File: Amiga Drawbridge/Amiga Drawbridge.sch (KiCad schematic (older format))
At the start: 13 parts, among them J1 FDC, J2 PWR_EXT, J3 PWR_DRV, J4 12v, M1 Mounting, M2 Mounting, M3 Mounting, M4 Mounting

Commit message: Added metal details
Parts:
- J1: footprint (none) -> Connector_IDC:IDC-Header_2x17_P2.54mm_Vertical
- J2: footprint (none) -> Connector_BarrelJack:BarrelJack_Horizontal
- J3: footprint (none) -> TerminalBlock:TerminalBlock_bornier-4_P5.08mm
- J4: footprint (none) -> Connector_PinSocket_2.54mm:PinSocket_1x01_P2.54mm_Vertical
- JP1, JP2: footprint (none) -> solder_bridge:select
- M1, M2, M3, M4: footprint (none) -> mounting:M3
- R1: footprint (none) -> Resistor_THT:R_Axial_DIN0207_L6.3mm_D2.5mm_P10.16mm_Horizontal
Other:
- note added: "Arduino pin order (A or B):\n1-2 DTR TXO RXI VCC GND GND\n2-3 GND GND VCC RXI TXO DTR"
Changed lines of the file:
@@
 F 0 "J1" H 10050 4865 50  0000 C CNN
 F 1 "FDC" H 10050 4774 50  0000 C CNN
-F 2 "" H 10150 3825 50  0001 C CNN
+F 2 "Connector_IDC:IDC-Header_2x17_P2.54mm_Vertical" H 10150 3825 50  0001 C CNN
 F 3 "~" H 10150 3825 50  0001 C CNN
 	1    10050 3825
@@
 F 0 "R1" H 9234 2896 50  0000 L CNN
 F 1 "1k" H 9234 2805 50  0000 L CNN
-F 2 "" H 9175 2850 50  0001 C CNN
+F 2 "Resistor_THT:R_Axial_DIN0207_L6.3mm_D2.5mm_P10.16mm_Horizontal" H 9175 2850 50  0001 C CNN
 F 3 "~" H 9175 2850 50  0001 C CNN
 	1    9175 2850
@@
 F 0 "JP1" H 6625 3011 50  0000 C CNN
 F 1 "ARD_TYPE" H 6625 3102 50  0000 C CNN
-F 2 "" H 6625 2900 50  0001 C CNN
+F 2 "solder_bridge:select" H 6625 2900 50  0001 C CNN
 F 3 "~" H 6625 2900 50  0001 C CNN
 	1    6625 2900
@@
 F 0 "M1" H 10750 675 50  0001 C CNN
 F 1 "Mounting" H 10750 500 50  0001 C CNN
-F 2 "" H 10750 575 50  0001 C CNN
+F 2 "mounting:M3" H 10750 575 50  0001 C CNN
 F 3 "~" H 10750 575 50  0001 C CNN
 	1    10750 575
@@
 F 0 "M2" H 10875 675 50  0001 C CNN
 F 1 "Mounting" H 10875 500 50  0001 C CNN
-F 2 "" H 10875 575 50  0001 C CNN
+F 2 "mounting:M3" H 10875 575 50  0001 C CNN
 F 3 "~" H 10875 575 50  0001 C CNN
 	1    10875 575
@@
 F 0 "M3" H 11000 675 50  0001 C CNN
 F 1 "Mounting" H 11000 500 50  0001 C CNN
-F 2 "" H 11000 575 50  0001 C CNN
+F 2 "mounting:M3" H 11000 575 50  0001 C CNN
 F 3 "~" H 11000 575 50  0001 C CNN
 	1    11000 575
@@
 F 0 "M4" H 11125 675 50  0001 C CNN
 F 1 "Mounting" H 11125 500 50  0001 C CNN
-F 2 "" H 11125 575 50  0001 C CNN
+F 2 "mounting:M3" H 11125 575 50  0001 C CNN
 F 3 "~" H 11125 575 50  0001 C CNN
 	1    11125 575
@@
 F 0 "J3" H 3398 6666 50  0000 L CNN
 F 1 "PWR_DRV" H 3398 6575 50  0000 L CNN
-F 2 "" H 3050 6675 50  0001 C CNN
+F 2 "TerminalBlock:TerminalBlock_bornier-4_P5.08mm" H 3050 6675 50  0001 C CNN
 F 3 "~" H 3050 6675 50  0001 C CNN
 	1    3050 6675
@@
 F 0 "J2" H 1882 6392 50  0000 C CNN
 F 1 "PWR_EXT" H 1882 6301 50  0000 C CNN
-F 2 "" H 1875 6035 50  0001 C CNN
+F 2 "Connector_BarrelJack:BarrelJack_Horizontal" H 1875 6035 50  0001 C CNN
 F 3 "~" H 1875 6035 50  0001 C CNN
 	1    1825 6075
@@
 F 0 "JP2" H 2525 6179 50  0000 C CNN
 F 1 "PWR_SEL" H 2525 6088 50  0000 C CNN
-F 2 "" H 2525 5975 50  0001 C CNN
+F 2 "solder_bridge:select" H 2525 5975 50  0001 C CNN
 F 3 "~" H 2525 5975 50  0001 C CNN
 	1    2525 5975
@@
 Wire Wire Line
 	2200 6775 2200 7000
-Wire Bus Line
-	4050 2100 4050 3825
-Wire Bus Line
-	8150 2100 8150 4525
-Wire Bus Line
-	4800 2100 4800 4525
-Wire Bus Line
-	8925 2100 8925 4525
 $Comp
 L Connector_Generic:Conn_01x01 J4
@@
 F 0 "J4" H 2730 6917 50  0000 L CNN
 F 1 "12v" H 2730 6826 50  0000 L CNN
-F 2 "" H 2650 6875 50  0001 C CNN
+F 2 "Connector_PinSocket_2.54mm:PinSocket_1x01_P2.54mm_Vertical" H 2650 6875 50  0001 C CNN
 F 3 "~" H 2650 6875 50  0001 C CNN
 	1    2650 6875
 	-1   0    0    1
 $EndComp
+Text Notes 6900 3175 0    50   ~ 0
+Arduino pin order (A or B):\n1-2 DTR TXO RXI VCC GND GND\n2-3 GND GND VCC RXI TXO DTR
+Wire Bus Line
+	4050 2100 4050 3825
+Wire Bus Line
+	8150 2100 8150 4525
+Wire Bus Line
+	4800 2100 4800 4525
+Wire Bus Line
+	8925 2100 8925 4525
 $EndSCHEMATC

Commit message: Arduino Pro Mini footprint
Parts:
- A1: footprint (none) -> arduino:Arduino_Pro_Mini
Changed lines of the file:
@@
 F 0 "A1" H 6525 4025 50  0000 C CNN
 F 1 "Arduino_Pro_Mini" H 6525 3925 50  0000 C CNN
-F 2 "" H 6475 4025 50  0001 C CNN
+F 2 "arduino:Arduino_Pro_Mini" H 6475 4025 50  0001 C CNN
 F 3 "~" H 6475 4025 50  0001 C CNN
 	1    6525 4025

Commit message: Routed tracks
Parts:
- A2: footprint (none) -> ft232rl:FT232RL
- J3: footprint TerminalBlock:TerminalBlock_bornier-4_P5.08mm -> pwr_drv:PWR_DRV
- J4: footprint Connector_PinSocket_2.54mm:PinSocket_1x01_P2.54mm_Vertical -> Connector_PinHeader_2.54mm:PinHeader_1x01_P2.54mm_Vertical
- M1, M2, M3, M4: footprint mounting:M3 -> mounting:M3_pin
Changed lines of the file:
@@
 F 0 "A2" H 2400 4415 50  0000 C CNN
 F 1 "FT232RL" H 2400 4324 50  0000 C CNN
-F 2 "" H 1950 3775 50  0001 C CNN
+F 2 "ft232rl:FT232RL" H 1950 3775 50  0001 C CNN
 F 3 "~" H 1950 3775 50  0001 C CNN
 	1    2400 3525
@@
 F 0 "M1" H 10750 675 50  0001 C CNN
 F 1 "Mounting" H 10750 500 50  0001 C CNN
-F 2 "mounting:M3" H 10750 575 50  0001 C CNN
+F 2 "mounting:M3_pin" H 10750 575 50  0001 C CNN
 F 3 "~" H 10750 575 50  0001 C CNN
 	1    10750 575
@@
 F 0 "M2" H 10875 675 50  0001 C CNN
 F 1 "Mounting" H 10875 500 50  0001 C CNN
-F 2 "mounting:M3" H 10875 575 50  0001 C CNN
+F 2 "mounting:M3_pin" H 10875 575 50  0001 C CNN
 F 3 "~" H 10875 575 50  0001 C CNN
 	1    10875 575
@@
 F 0 "M3" H 11000 675 50  0001 C CNN
 F 1 "Mounting" H 11000 500 50  0001 C CNN
-F 2 "mounting:M3" H 11000 575 50  0001 C CNN
+F 2 "mounting:M3_pin" H 11000 575 50  0001 C CNN
 F 3 "~" H 11000 575 50  0001 C CNN
 	1    11000 575
@@
 F 0 "M4" H 11125 675 50  0001 C CNN
 F 1 "Mounting" H 11125 500 50  0001 C CNN
-F 2 "mounting:M3" H 11125 575 50  0001 C CNN
+F 2 "mounting:M3_pin" H 11125 575 50  0001 C CNN
 F 3 "~" H 11125 575 50  0001 C CNN
 	1    11125 575
@@
 F 0 "J3" H 3398 6666 50  0000 L CNN
 F 1 "PWR_DRV" H 3398 6575 50  0000 L CNN
-F 2 "TerminalBlock:TerminalBlock_bornier-4_P5.08mm" H 3050 6675 50  0001 C CNN
+F 2 "pwr_drv:PWR_DRV" H 3050 6675 50  0001 C CNN
 F 3 "~" H 3050 6675 50  0001 C CNN
 	1    3050 6675
@@
 F 0 "J4" H 2730 6917 50  0000 L CNN
 F 1 "12v" H 2730 6826 50  0000 L CNN
-F 2 "Connector_PinSocket_2.54mm:PinSocket_1x01_P2.54mm_Vertical" H 2650 6875 50  0001 C CNN
+F 2 "Connector_PinHeader_2.54mm:PinHeader_1x01_P2.54mm_Vertical" H 2650 6875 50  0001 C CNN
 F 3 "~" H 2650 6875 50  0001 C CNN
 	1    2650 6875

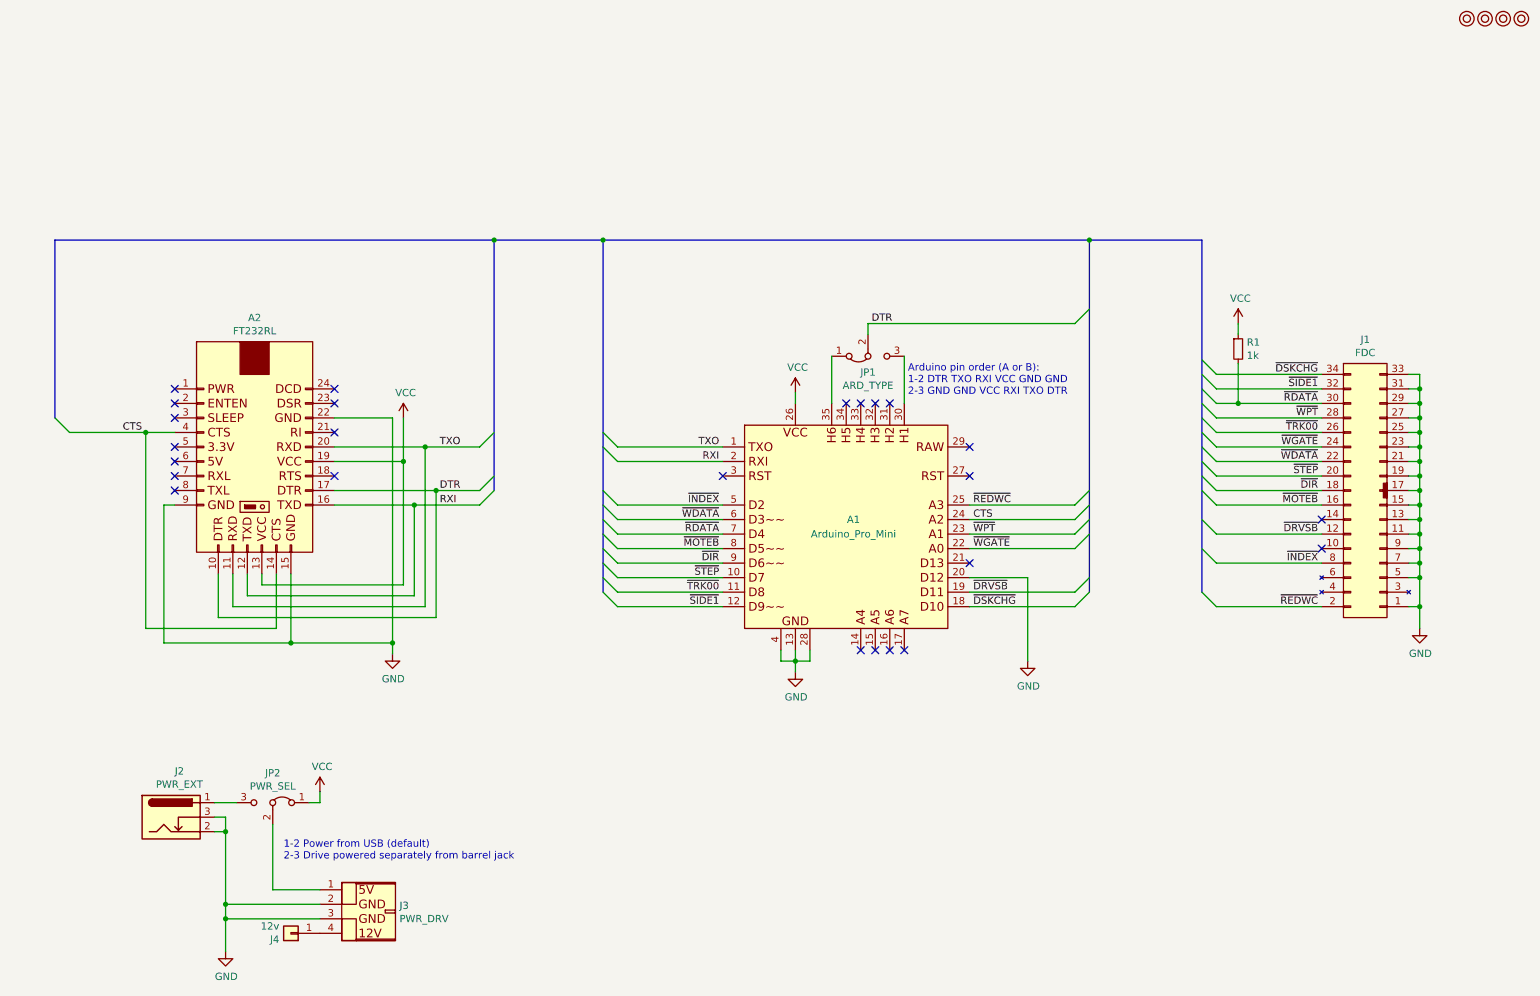
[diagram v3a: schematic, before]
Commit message: Added LEDs and moved connectors
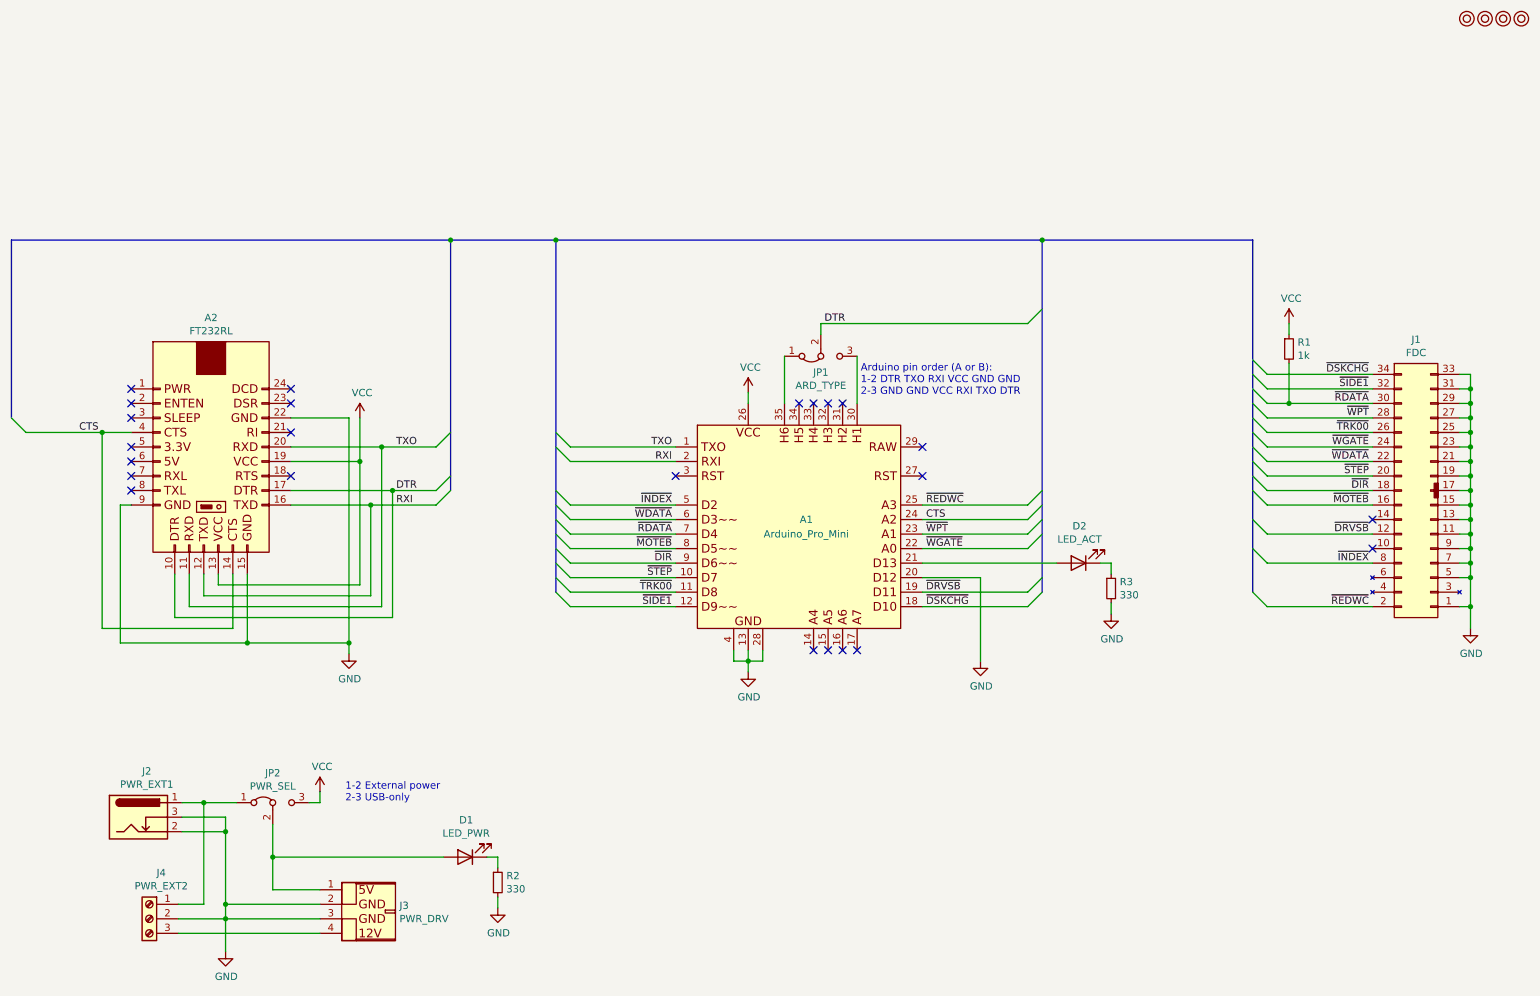
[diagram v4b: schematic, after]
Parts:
- removed J4: 12v, Connector_PinHeader_2.54mm:PinHeader_1x01_P2.54mm_Vertical, symbol Connector_Generic:Conn_01x01
- added D1: LED_PWR, LED_THT:LED_D5.0mm, symbol Device:LED
- added D2: LED_ACT, LED_THT:LED_D5.0mm, symbol Device:LED
- added J4: PWR_EXT2, pwr_drv:PWR_EXT, symbol Connector:Screw_Terminal_01x03
- added R2, R3: 330, Resistor_THT:R_Axial_DIN0207_L6.3mm_D2.5mm_P10.16mm_Horizontal, symbol Device:R_Small
- J2: value PWR_EXT -> PWR_EXT1
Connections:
- net GND: now also J4.2 (Pin_2), R2.2, R3.2
- net VCC: now also JP2.3 (B); no longer JP2.1 (A)
- net at A1.21 (D13): now also D2.2 (A)
- net at J3.1 (Pin_1), JP2.2 (C): now also D1.2 (A)
- net at J3.4 (Pin_4): now also J4.3 (Pin_3)
- net at J2.1: now also JP2.1 (A), J4.1 (Pin_1); no longer JP2.3 (B)
- new net: D1.1 (K), R2.1
- new net: D2.1 (K), R3.1
- no-connect marks 25 -> 24
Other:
- note added: "1-2 External power\n2-3 USB-only"
- note removed: "1-2 Power from USB (default)\n2-3 Drive powered separately from barrel jack"
- moved on the sheet: A1, A2, J1, J2, JP1, R1
